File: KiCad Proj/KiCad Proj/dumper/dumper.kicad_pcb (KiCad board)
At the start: 2 copper layers, 78.7 x 87.6 mm, 27 parts, among them J1 CartBus, J2 SPI, K1 G6K-2, SW2 SW_SPST, SW3 SW_SPST, SW4 KFC-C-15A, U1 74HC595, U2 SN74LVC8T245PWR, U3 74HC595, U4 SN74LVC8T245PWR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

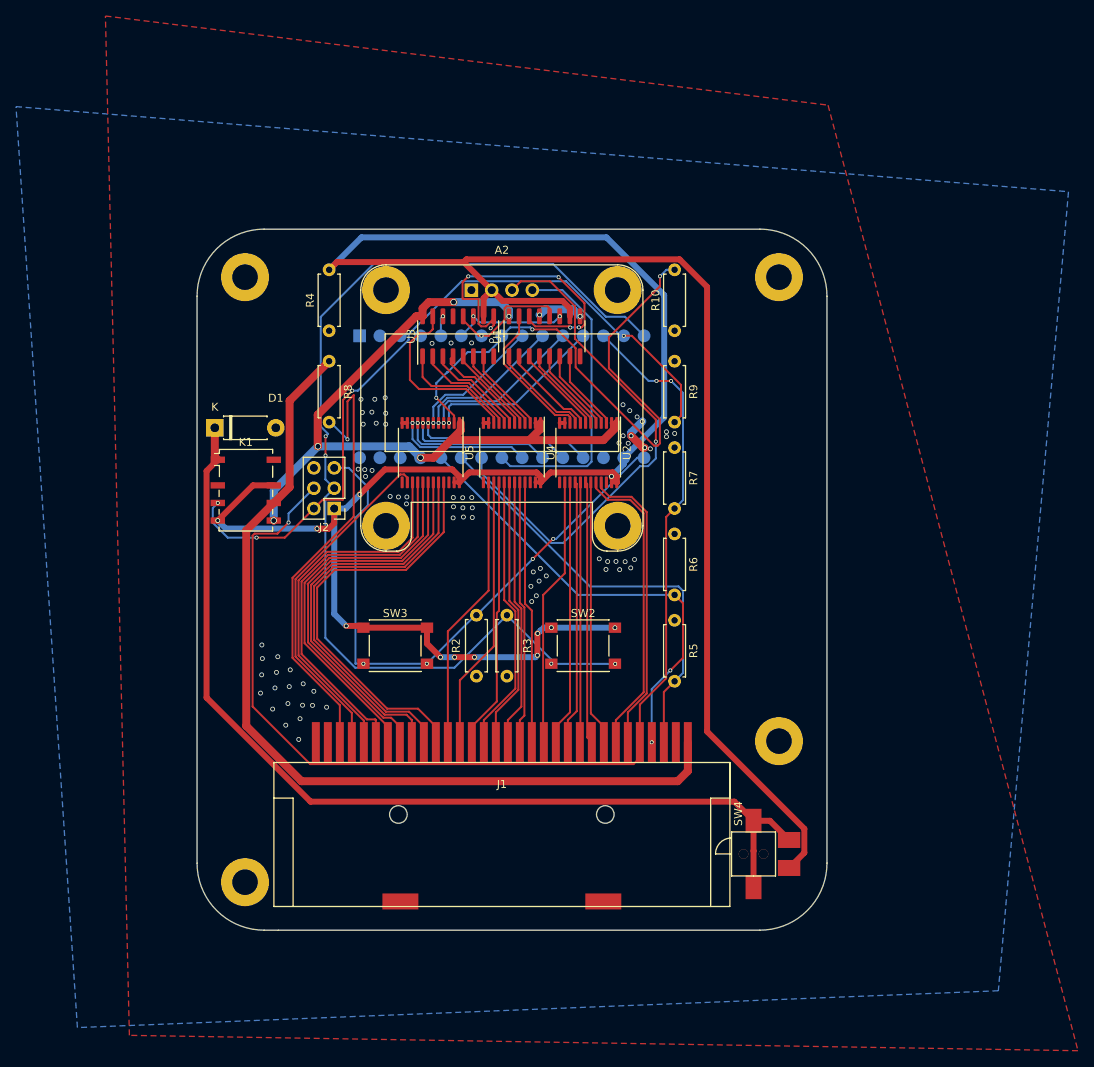
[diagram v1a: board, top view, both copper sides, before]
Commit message: Fixed up the schematic and PCB for two very severe omissions
I forgot to translate the WR, RD, and CS pins and added a transceiver for those

I also forgot that the transceivers should have CART_VCC on VccB
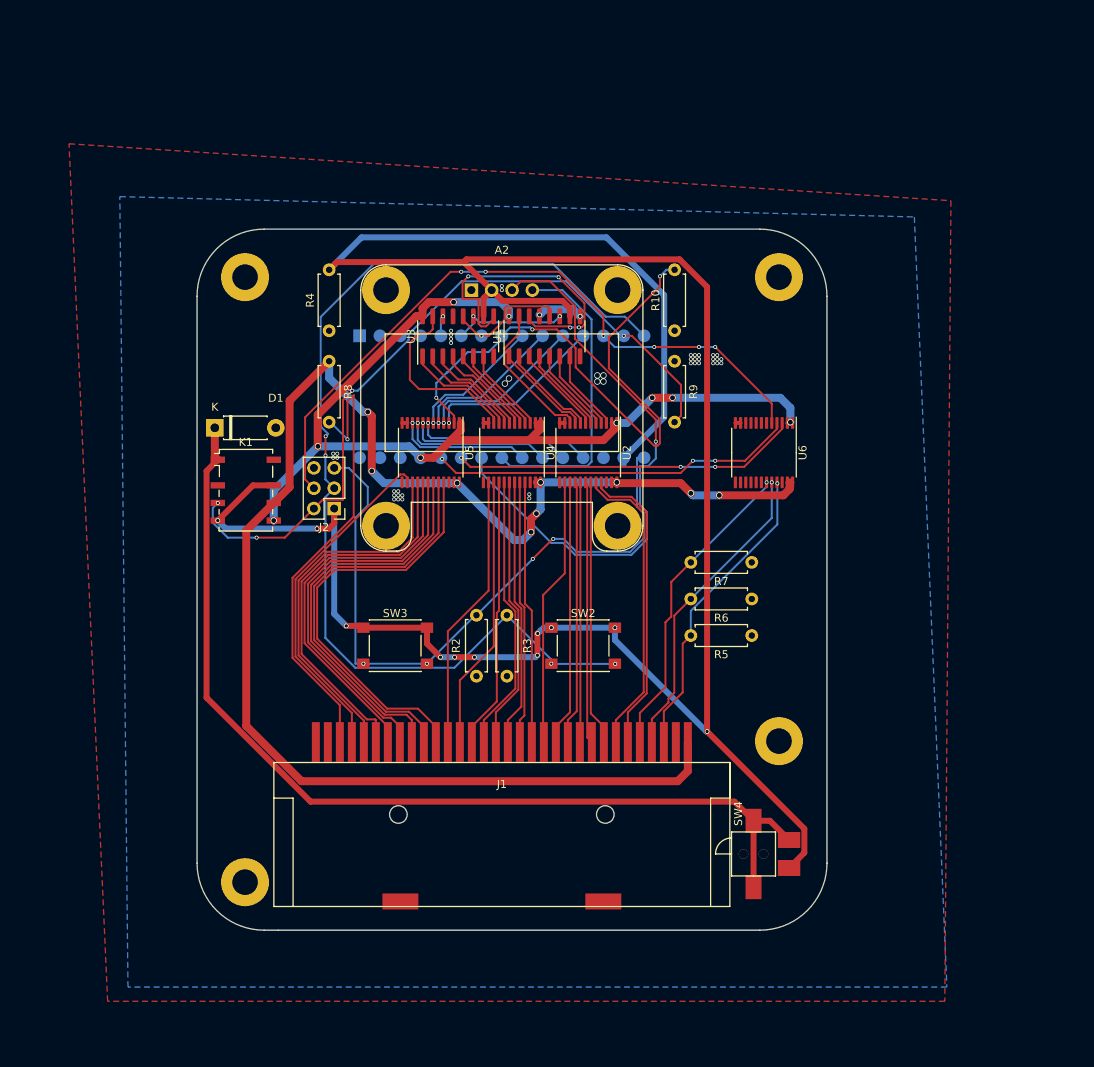
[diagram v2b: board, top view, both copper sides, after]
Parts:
- added U6: SN74LVC8T245PWR, Package_SO:TSSOP-24_6.1x7.8mm_P0.65mm, F.Cu at (200.4, 81.3)
- moved R7 17.3 mm to (198.9, 95.0), turned to 180 degrees
- moved R6 12.6 mm to (198.9, 99.6), turned to 180 degrees
- moved R5 9.84 mm to (198.9, 104.1), turned to 180 degrees
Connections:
- A1 pad 13: /Cartridge Slot/CART_CS -> /Controller/CART_CS
- A1 pad 25: /Cartridge Slot/CART_WR -> /Controller/CART_WR
- A1 pad 26: /Cartridge Slot/CART_RD -> /Controller/CART_RD
- J1 pad 3: /Cartridge Slot/CART_WR -> /Cartridge Slot/TRANS_CART_WR
- J1 pad 4: /Cartridge Slot/CART_RD -> /Cartridge Slot/TRANS_CART_RD
- J1 pad 5: /Cartridge Slot/CART_CS -> /Cartridge Slot/TRANS_CART_CS
- J2 pad 4: /Cartridge Slot/CART_CS -> /Controller/CART_CS
- R5 pad 2: /Cartridge Slot/CART_WR -> /Cartridge Slot/TRANS_CART_WR
- R6 pad 2: /Cartridge Slot/CART_RD -> /Cartridge Slot/TRANS_CART_RD
- R7 pad 2: /Cartridge Slot/CART_CS -> /Cartridge Slot/TRANS_CART_CS
- U2 pad 23: +3V3 -> /Cart Detection/CART_VCC
- U2 pad 24: +3V3 -> /Cart Detection/CART_VCC
- U4 pad 23: +3V3 -> /Cart Detection/CART_VCC
- U4 pad 24: +3V3 -> /Cart Detection/CART_VCC
- U5 pad 23: +3V3 -> /Cart Detection/CART_VCC
- U5 pad 24: +3V3 -> /Cart Detection/CART_VCC
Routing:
- net /Cartridge Slot/CART_CS: track 144.6 -> 0.00 mm, vias 3 -> 0
- net /Controller/CART_CS: track 0.00 -> 85.9 mm, vias 0 -> 6
- net /Cart Detection/CART_VCC: track 112.1 -> 194.2 mm, vias 0 -> 9
- net /Cartridge Slot/CART_RD: track 56.8 -> 0.00 mm, vias 2 -> 0
- net /Cartridge Slot/CART_WR: track 54.5 -> 0.00 mm
- net /Controller/CART_RD: track 0.00 -> 45.6 mm, vias 0 -> 3
- net /Controller/CART_WR: track 0.00 -> 43.3 mm, vias 0 -> 3
- net /Cartridge Slot/TRANS_CART_CS: track 0.00 -> 39.0 mm, vias 0 -> 1
- net /Cartridge Slot/TRANS_CART_RD: track 0.00 -> 38.7 mm, vias 0 -> 1
- net /Cartridge Slot/TRANS_CART_WR: track 0.00 -> 38.2 mm, vias 0 -> 1
- net +3V3: track 345.0 -> 316.3 mm, vias 12 -> 11
- net +5V: track 93.7 -> 119.7 mm, vias 5 -> 9
- net /Controller/SCK: track 74.7 -> 83.4 mm
- net /Controller/SCL: track 64.5 -> 72.3 mm
- net GND: track 12.4 -> 8.32 mm, vias 79 -> 45
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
